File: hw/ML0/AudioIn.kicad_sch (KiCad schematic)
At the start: 32 parts, among them T2 Transformer_1P_1S, U5 LMV321, U6 LMV321, U7 LMV321, U8 LMV321

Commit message: Working on V0 of the analog PCB
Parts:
- removed C23, C28, C31: 470u, symbol Device:C_Polarized_US
- removed C25, C30, C32: 0.1u, symbol Device:C
- removed U5, U6, U7, U8: LMV321, symbol Amplifier_Operational:LMV321
- added U9: LMV324, symbol Amplifier_Operational:LMV324
- R18: value 1k -> 0R
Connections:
- net +3.3VA: now also U9.4 (V+)
- net GNDA: now also U9.11 (V-)
- net at C17.2, C18.1, R10.2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: now also U9.3 (+)
- net at C26.2, R18.1: now also U9.6 (-), U9.7
- net at C27.1, R17.2: now also U9.5 (+)
- net at C22.2, R13.2, R15.2: now also U9.1, U9.10 (+)
- net at C29.1, RV4.2: now also U9.13 (-)
- net at C22.1, R12.2, R13.1: now also U9.2 (-)
- net at R14.2, R16.1: now also U9.9 (-)
- net at R16.2: now also U9.12 (+), U9.8
- new net GPIO_COS: U9.14
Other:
- note added: "Caculate correct ratio when we swtich to 3.0V ADC VREF"
- moved on the sheet: C20, C21

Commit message: Working on PCB 0
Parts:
- C17, C18, C21, C22, C26, C27, C29: footprint (none) -> Capacitor_SMD:C_0805_2012Metric_Pad1.18x1.45mm_HandSolder
- C19, C20, C24: footprint (none) -> Capacitor_SMD:CP_Elec_8x10
- R10, R11, R12, R13, R14, R16, R18: footprint (none) -> Resistor_SMD:R_0805_2012Metric_Pad1.20x1.40mm_HandSolder
- R15: value 2.2k -> 1.5k; footprint (none) -> Resistor_SMD:R_0805_2012Metric_Pad1.20x1.40mm_HandSolder
- R17: value 3.9k -> 2.7k; footprint (none) -> Resistor_SMD:R_0805_2012Metric_Pad1.20x1.40mm_HandSolder
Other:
- note added: "Anti-Aliasing LPF Filter fc = 4kHz"
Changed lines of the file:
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@@
+    (effects (font (size 1.27 1.27)) (justify left bottom))
+  )
+  (text "Anti-Aliasing LPF Filter\nfc = 4kHz" (at 195.58 86.36 0)
     (effects (font (size 1.27 1.27)) (justify left bottom))
   )
@@
       (effects (font (size 1.27 1.27)) (justify left))
     )
-    (property "Footprint" "" (at 94.996 53.594 90)
+    (property "Footprint" "Resistor_SMD:R_0805_2012Metric_Pad1.20x1.40mm_HandSolder" (at 94.996 53.594 90)
       (effects (font (size 1.27 1.27)) hide)
     )
@@
       (effects (font (size 1.27 1.27)) (justify left))
     )
-    (property "Footprint" "" (at 164.7952 76.2 0)
+    (property "Footprint" "Capacitor_SMD:C_0805_2012Metric_Pad1.18x1.45mm_HandSolder" (at 164.7952 76.2 0)
       (effects (font (size 1.27 1.27)) hide)
     )
@@
       (effects (font (size 1.27 1.27)))
     )
-    (property "Footprint" "" (at 225.044 66.294 90)
+    (property "Footprint" "Resistor_SMD:R_0805_2012Metric_Pad1.20x1.40mm_HandSolder" (at 225.044 66.294 90)
       (effects (font (size 1.27 1.27)) hide)
     )
@@
       (effects (font (size 1.27 1.27)))
     )
-    (property "Value" "2.2k" (at 153.67 60.96 90)
-      (effects (font (size 1.27 1.27)))
-    )
-    (property "Footprint" "" (at 153.416 65.786 90)
+    (property "Value" "1.5k" (at 153.67 60.96 90)
+      (effects (font (size 1.27 1.27)))
+    )
+    (property "Footprint" "Resistor_SMD:R_0805_2012Metric_Pad1.20x1.40mm_HandSolder" (at 153.416 65.786 90)
       (effects (font (size 1.27 1.27)) hide)
     )
@@
       (effects (font (size 1.27 1.27)))
     )
-    (property "Value" "3.9k" (at 173.99 60.96 90)
-      (effects (font (size 1.27 1.27)))
-    )
-    (property "Footprint" "" (at 174.244 63.754 90)
+    (property "Value" "2.7k" (at 173.99 60.96 90)
+      (effects (font (size 1.27 1.27)))
+    )
+    (property "Footprint" "Resistor_SMD:R_0805_2012Metric_Pad1.20x1.40mm_HandSolder" (at 174.244 63.754 90)
       (effects (font (size 1.27 1.27)) hide)
     )
@@
       (effects (font (size 1.27 1.27)) (justify left))
     )
-    (property "Footprint" "" (at 205.4352 156.21 0)
+    (property "Footprint" "Capacitor_SMD:C_0805_2012Metric_Pad1.18x1.45mm_HandSolder" (at 205.4352 156.21 0)
       (effects (font (size 1.27 1.27)) hide)
     )
@@
       (effects (font (size 1.27 1.27)))
     )
-    (property "Footprint" "" (at 127 54.61 0)
+    (property "Footprint" "Capacitor_SMD:C_0805_2012Metric_Pad1.18x1.45mm_HandSolder" (at 127 54.61 0)
       (effects (font (size 1.27 1.27)) hide)
     )
@@
       (effects (font (size 1.27 1.27)) (justify right))
     )
-    (property "Footprint" "" (at 109.474 77.216 90)
+    (property "Footprint" "Resistor_SMD:R_0805_2012Metric_Pad1.20x1.40mm_HandSolder" (at 109.474 77.216 90)
       (effects (font (size 1.27 1.27)) hide)
     )
@@
       (effects (font (size 1.27 1.27)))
     )
-    (property "Footprint" "" (at 91.44 61.2648 0)
+    (property "Footprint" "Capacitor_SMD:C_0805_2012Metric_Pad1.18x1.45mm_HandSolder" (at 91.44 61.2648 0)
       (effects (font (size 1.27 1.27)) hide)
     )
@@
       (effects (font (size 1.27 1.27)) (justify left))
     )
-    (property "Footprint" "" (at 94.996 70.104 90)
+    (property "Footprint" "Resistor_SMD:R_0805_2012Metric_Pad1.20x1.40mm_HandSolder" (at 94.996 70.104 90)
       (effects (font (size 1.27 1.27)) hide)
     )
@@
       (effects (font (size 1.27 1.27)) (justify right))
     )
-    (property "Footprint" "" (at 148.844 153.416 90)
+    (property "Footprint" "Resistor_SMD:R_0805_2012Metric_Pad1.20x1.40mm_HandSolder" (at 148.844 153.416 90)
       (effects (font (size 1.27 1.27)) hide)
     )
@@
       (effects (font (size 1.27 1.27)) (justify left))
     )
-    (property "Footprint" "" (at 240.9952 38.1 0)
+    (property "Footprint" "Capacitor_SMD:C_0805_2012Metric_Pad1.18x1.45mm_HandSolder" (at 240.9952 38.1 0)
       (effects (font (size 1.27 1.27)) hide)
     )
@@
       (effects (font (size 1.27 1.27)) (justify left))
     )
-    (property "Footprint" "" (at 182.5752 87.63 0)
+    (property "Footprint" "Capacitor_SMD:C_0805_2012Metric_Pad1.18x1.45mm_HandSolder" (at 182.5752 87.63 0)
       (effects (font (size 1.27 1.27)) hide)
     )
@@
       (effects (font (size 1.27 1.27)) (justify left))
     )
-    (property "Footprint" "" (at 110.49 88.9 0)
+    (property "Footprint" "Capacitor_SMD:CP_Elec_8x10" (at 110.49 88.9 0)
       (effects (font (size 1.27 1.27)) hide)
     )
@@
       (effects (font (size 1.27 1.27)))
     )
-    (property "Footprint" "" (at 166.624 123.444 90)
+    (property "Footprint" "Resistor_SMD:R_0805_2012Metric_Pad1.20x1.40mm_HandSolder" (at 166.624 123.444 90)
       (effects (font (size 1.27 1.27)) hide)
     )
@@
       (effects (font (size 1.27 1.27)) (justify left))
     )
-    (property "Footprint" "" (at 149.86 165.1 0)
+    (property "Footprint" "Capacitor_SMD:CP_Elec_8x10" (at 149.86 165.1 0)
       (effects (font (size 1.27 1.27)) hide)
     )
@@
       (effects (font (size 1.27 1.27)))
     )
-    (property "Footprint" "" (at 127.254 47.244 90)
+    (property "Footprint" "Resistor_SMD:R_0805_2012Metric_Pad1.20x1.40mm_HandSolder" (at 127.254 47.244 90)
       (effects (font (size 1.27 1.27)) hide)
     )
@@
       (effects (font (size 1.27 1.27)) (justify left))
     )
-    (property "Footprint" "" (at 101.2952 80.01 0)
+    (property "Footprint" "Capacitor_SMD:C_0805_2012Metric_Pad1.18x1.45mm_HandSolder" (at 101.2952 80.01 0)
       (effects (font (size 1.27 1.27)) hide)
     )
@@
       (effects (font (size 1.27 1.27)) (justify left))
     )
-    (property "Footprint" "" (at 227.33 34.29 0)
-      (effects (font (size 1.27 1.27)) hide)
-    )
+    (property "Footprint" "Capacitor_SMD:CP_Elec_8x10" (at 227.33 34.29 0)
+      (effects (font (size 1.27 1.27)) hide)
+    )

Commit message: Docs
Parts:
- added R8: 0R, Resistor_SMD:R_0805_2012Metric_Pad1.20x1.40mm_HandSolder, symbol Device:R_US
- added R9: 1k, Resistor_SMD:R_0805_2012Metric_Pad1.20x1.40mm_HandSolder, symbol Device:R_US
- added U5: LTV-356T, Package_SO:SO-4_4.4x3.6mm_P2.54mm, symbol Isolator:LTV-356T
- RV3, RV4: footprint (none) -> Potentiometer_SMD:Potentiometer_Bourns_3314S_Horizontal
- T2: footprint (none) -> Capacitor_SMD:CP_Elec_5x5.3
- U9: footprint (none) -> Package_SO:TSSOP-14_4.4x5mm_P0.65mm
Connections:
- net +3.3VA: now also R9.1
- net GNDA: now also U5.3
- net GPIO_COS: now also R9.2, U5.4
- net RIG_GND: now also U5.2
- new net: R8.2, U5.1
- new net RIG_COS: R8.1

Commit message: Initial layout done
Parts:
- added J5: Conn_01x03, Connector_PinHeader_2.54mm:PinHeader_1x03_P2.54mm_Vertical, symbol Connector_Generic:Conn_01x03
- C19, C24: footprint Capacitor_SMD:CP_Elec_8x10 -> KiCad-Library:CAP_KEMET_530_530
- C20: value 470u -> 100u; footprint Capacitor_SMD:CP_Elec_8x10 -> KiCad-Library:CAP_KEMET_530_530
- T2: footprint Capacitor_SMD:CP_Elec_5x5.3 -> KiCad-Library:CheapAudioTransformer
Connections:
- net RIG_AF_IN is gone; now on net GNDA: T2.1 (AA)
- net GNDA: no longer T2.3 (SA)
- net GPIO_COS: now also J5.2 (Pin_2); no longer R9.2, U5.4, U9.14
- net RIG_GND: no longer T2.2 (AB)
- net at C17.2, C18.1, R10.2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: now also U9.10 (+); no longer U9.3 (+)
- net at C22.2, R13.2, R15.2: now also U9.12 (+), U9.8; no longer U9.1, U9.10 (+)
- net at R14.2, R16.1: now also U9.13 (-); no longer U9.9 (-)
- net at C29.1, RV4.2: now also U9.2 (-); no longer U9.13 (-)
- net at C22.1, R12.2, R13.1: now also U9.9 (-); no longer U9.2 (-)
- net at RV3.1: now also T2.2 (AB); no longer T2.4 (SB)
- new net: J5.1 (Pin_1), R9.2, U5.4
- new net: J5.3 (Pin_3), U9.1
- new net: R16.2, U9.14, U9.3 (+)
- new net RIG_AF_OUT+: T2.3 (SA)
- new net RIG_AF_OUT-: T2.4 (SB)
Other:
- note added: "Jumper to control COS source"
- moved on the sheet: T2, U9A, U9C, U9D

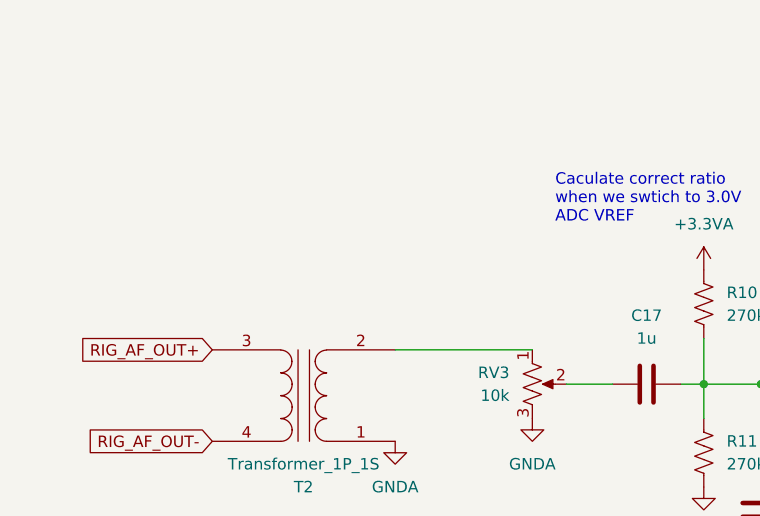
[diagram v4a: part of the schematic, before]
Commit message: Board sent to JLC on 2024-02-26 09:18 EST
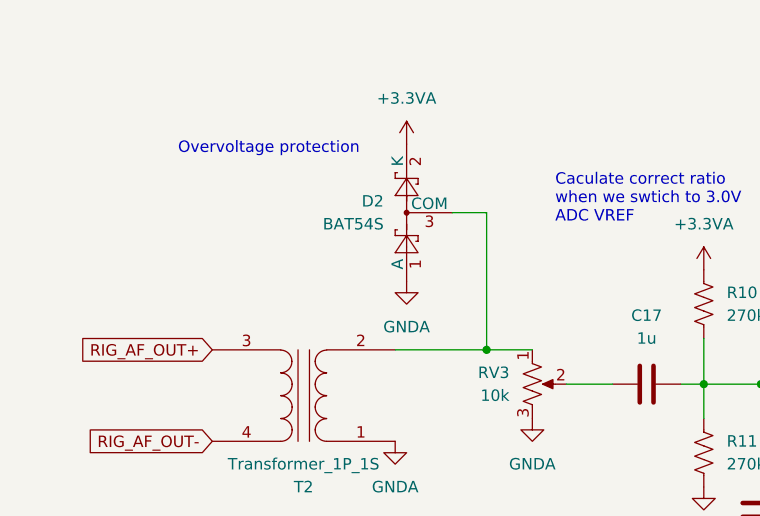
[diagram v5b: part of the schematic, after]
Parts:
- added D2: BAT54S, Package_TO_SOT_SMD:SOT-23, symbol Diode:BAT54S
- RV3, RV4: footprint Potentiometer_SMD:Potentiometer_Bourns_3314S_Horizontal -> KiCad-Library:POT_3362P
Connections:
- net +3.3VA: now also D2.2 (K)
- net GNDA: now also D2.1 (A)
- net at RV3.1, T2.2 (AB): now also D2.3 (COM)
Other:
- note added: "Overvoltage protection"
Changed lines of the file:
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@@
   (junction (at 110.49 54.61) (diameter 0) (color 0 0 0 0)
   )
+  (junction (at 69.85 58.42) (diameter 0) (color 0 0 0 0)
+  )
   (junction (at 137.16 64.77) (diameter 0) (color 0 0 0 0)
   )
@@
     (stroke (width 0) (type default))
   )
+  (wire (pts (xy 69.85 58.42) (xy 74.93 58.42))
+    (stroke (width 0) (type default))
+  )
   (wire (pts (xy 177.8 64.77) (xy 181.61 64.77))
     (stroke (width 0) (type default))
@@
     (stroke (width 0) (type default))
   )
-  (wire (pts (xy 59.69 58.42) (xy 74.93 58.42))
+  (wire (pts (xy 59.69 58.42) (xy 69.85 58.42))
     (stroke (width 0) (type default))
   )
@@
     (stroke (width 0) (type default))
   )
+  (wire (pts (xy 69.85 43.18) (xy 69.85 58.42))
+    (stroke (width 0) (type default))
+  )
   (wire (pts (xy 110.49 54.61) (xy 124.46 54.61))
     (stroke (width 0) (type default))
@@
   )
   (wire (pts (xy 149.86 143.51) (xy 149.86 124.46))
+    (stroke (width 0) (type default))
+  )
+  (wire (pts (xy 66.04 43.18) (xy 69.85 43.18))
     (stroke (width 0) (type default))
   )
@@
     (stroke (width 0) (type dot) (color 255 55 72 1))
     (fill (type none))
+  )
+  (text "Overvoltage protection" (at 35.56 36.83 0)
+    (effects (font (size 1.27 1.27)) (justify left bottom))
   )
   (text "Amplifier for \nCOS Detector" (at 130.81 147.32 0)
@@
     )
   )
+  (symbol (lib_id "power:GNDA") (at 60.96 50.8 0) (unit 1)
+    (in_bom yes) (on_board yes) (dnp no) (fields_autoplaced)
+    (property "Reference" "#PWR07" (at 60.96 57.15 0)
+      (effects (font (size 1.27 1.27)) hide)
+    )
+    (property "Value" "GNDA" (at 60.96 55.88 0)
+      (effects (font (size 1.27 1.27)))
+    )
+    (property "Footprint" "" (at 60.96 50.8 0)
+      (effects (font (size 1.27 1.27)) hide)
+    )
+    (property "Datasheet" "" (at 60.96 50.8 0)
+      (effects (font (size 1.27 1.27)) hide)
+    )
+    (pin "1")
+    (instances
+      (project "ML0"
+        (path "/5f8f636b-fd0e-498e-8696-0a023acb4c09/605cddf5-737f-47be-b5fd-7ed3decef4e0"
+          (reference "#PWR07") (unit 1)
+        )
+      )
+    )
+  )
   (symbol (lib_id "Device:Transformer_1P_1S") (at 49.53 63.5 180) (unit 1)
     (in_bom yes) (on_board yes) (dnp no)
@@
     )
   )
+  (symbol (lib_id "Diode:BAT54S") (at 60.96 43.18 90) (unit 1)
+    (in_bom yes) (on_board yes) (dnp no) (fields_autoplaced)
+    (property "Reference" "D2" (at 58.42 41.91 90)
+      (effects (font (size 1.27 1.27)) (justify left))
+    )
+    (property "Value" "BAT54S" (at 58.42 44.45 90)
+      (effects (font (size 1.27 1.27)) (justify left))
+    )
+    (property "Footprint" "Package_TO_SOT_SMD:SOT-23" (at 57.785 41.275 0)
+      (effects (font (size 1.27 1.27)) (justify left) hide)
+    )
+    (property "Datasheet" "https://www.diodes.com/assets/Datasheets/ds11005.pdf" (at 60.96 46.228 0)
+      (effects (font (size 1.27 1.27)) hide)
+    )
+    (pin "1")
+    (pin "2")
+    (pin "3")
+    (instances
+      (project "ML0"
+        (path "/5f8f636b-fd0e-498e-8696-0a023acb4c09/605cddf5-737f-47be-b5fd-7ed3decef4e0"
+          (reference "D2") (unit 1)
+        )
+      )
+    )
+  )
   (symbol (lib_id "Amplifier_Operational:LMV324") (at 212.09 35.56 0) (unit 5)
     (in_bom yes) (on_board yes) (dnp no) (fields_autoplaced)
@@
       (effects (font (size 1.27 1.27)) (justify right))
     )
-    (property "Footprint" "Potentiometer_SMD:Potentiometer_Bourns_3314S_Horizontal" (at 74.93 62.23 0)
+    (property "Footprint" "KiCad-Library:POT_3362P" (at 74.93 62.23 0)
       (effects (font (size 1.27 1.27)) hide)
     )
@@
       (effects (font (size 1.27 1.27)) (justify right))
     )
-    (property "Footprint" "Potentiometer_SMD:Potentiometer_Bourns_3314S_Horizontal" (at 198.12 146.05 0)
+    (property "Footprint" "KiCad-Library:POT_3362P" (at 198.12 146.05 0)
       (effects (font (size 1.27 1.27)) hide)
     )
@@
         )
       )
+    )
+  )
+  (symbol (lib_id "power:+3.3VA") (at 60.96 35.56 0) (unit 1)
+    (in_bom yes) (on_board yes) (dnp no) (fields_autoplaced)
+    (property "Reference" "#PWR040" (at 60.96 39.37 0)
+      (effects (font (size 1.27 1.27)) hide)
+    )
+    (property "Value" "+3.3VA" (at 60.96 30.48 0)
+      (effects (font (size 1.27 1.27)))
+    )
+    (property "Footprint" "" (at 60.96 35.56 0)
+      (effects (font (size 1.27 1.27)) hide)
+    )
+    (property "Datasheet" "" (at 60.96 35.56 0)
+      (effects (font (size 1.27 1.27)) hide)
+    )
+    (pin "1")
+    (instances
+      (project "ML0"
+        (path "/5f8f636b-fd0e-498e-8696-0a023acb4c09/605cddf5-737f-47be-b5fd-7ed3decef4e0"
+          (reference "#PWR040") (unit 1)
+        )
+      )
